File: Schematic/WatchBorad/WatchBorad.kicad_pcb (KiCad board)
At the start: 4 copper layers, 35 x 35 mm, 118 parts, among them J1 Conn_01x07_Female, J3 TYPE-C-31-M-17, M1 Motor_DC, SW1 SW_Push, SW2 SW_Push, SW3 SW_Push, SW4 SW_Push, SW5 SW_Push, U1 LSM6DSLTR, U10 TPS62740DSST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

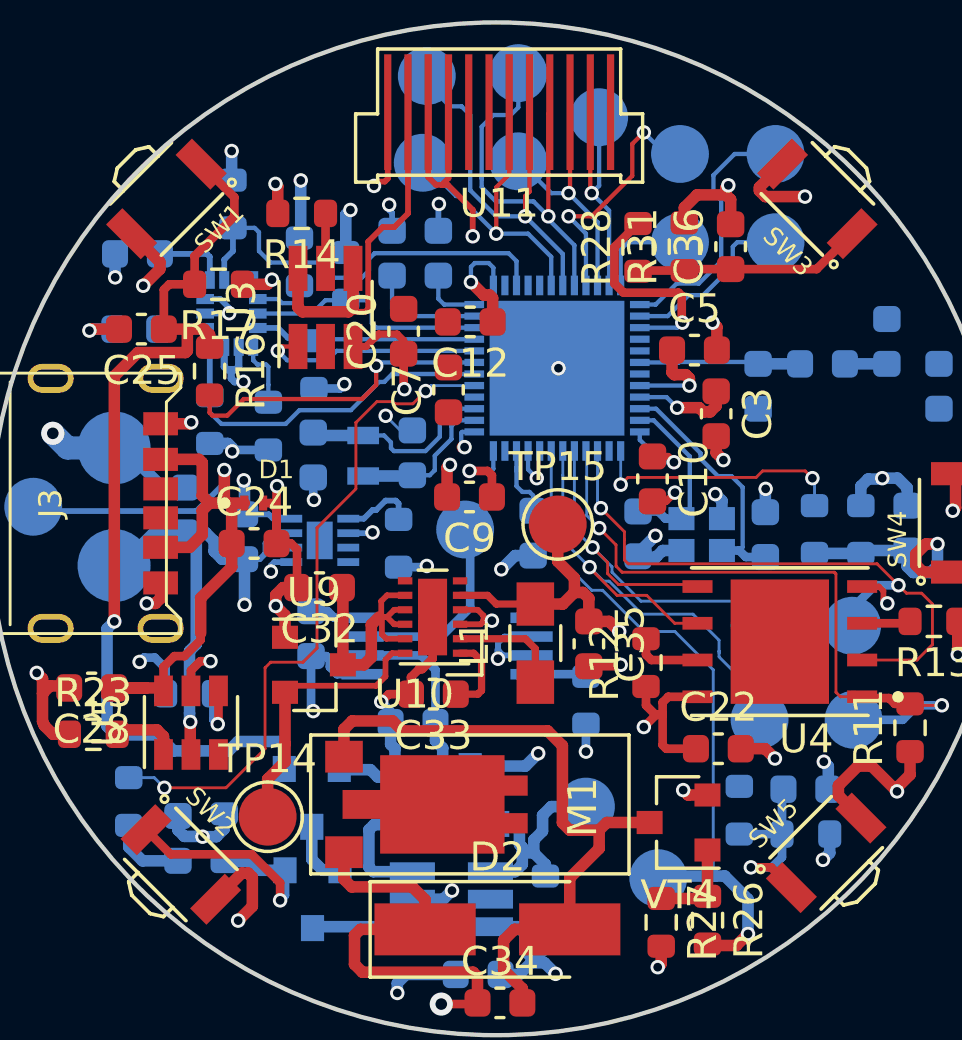
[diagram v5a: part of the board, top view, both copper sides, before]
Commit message: Fixed DRC warnings
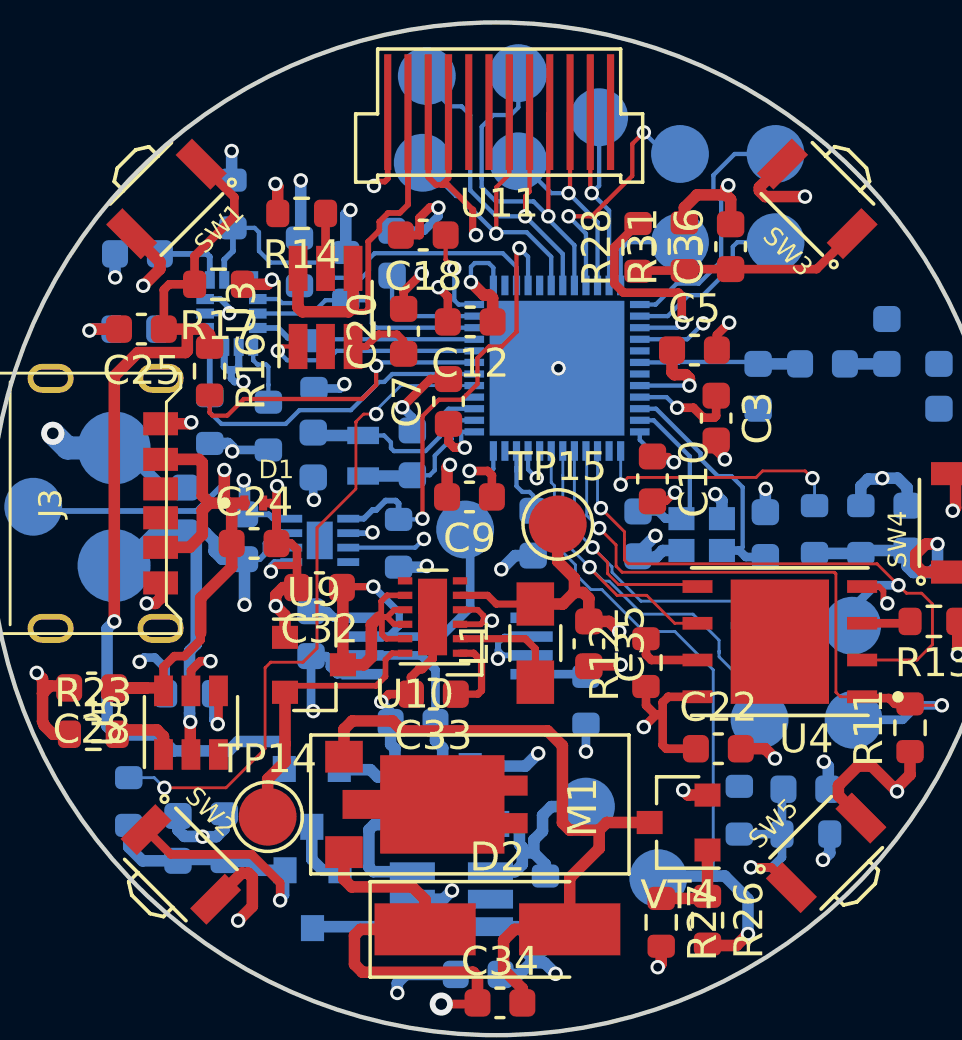
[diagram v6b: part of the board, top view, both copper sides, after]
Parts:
- C18: moved to F.Cu
- moved C18 0.82 mm to (86.4, 78.8), turned to 180 degrees
- moved C7 0.40 mm to (87.2, 84.5)
- moved C3 0.15 mm to (96.5, 85.1)
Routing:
- net /MCU/FG_OD_ALRT_N: track 2.59 -> 16.3 mm, vias 0 -> 2
- net GND: track 92.6 -> 100.4 mm, vias 48 -> 49
- net /DCDC&PB/DCDC_VIN: track 19.9 -> 24.2 mm, vias 0 -> 1
- net /MCU/SCL_FG: track 0.00 -> 2.74 mm, vias 0 -> 1
- net /MCU/SDA_FG: track 0.00 -> 2.42 mm, vias 0 -> 1
- net Net-(C26-Pad1): track 12.0 -> 13.6 mm
- net +3V3: track 180.8 -> 182.4 mm, vias 19 -> 18
- net /MCU/DEC1: track 1.20 -> 2.48 mm
- net /MCU/NFC2: track 2.12 -> 3.13 mm, vias 0 -> 1
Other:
- rule via_min_size: 0.4 -> 0.5

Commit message: Added RTC to the schematic and PCB lists [PCB]
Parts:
- added U12: M41T62Q6F, M41T62Q6F:QFN50P300X300X100-17N, F.Cu at (75.6, 68.2)
- added Y1: Crystal_Small, Crystal:Crystal_SMD_3215-2Pin_3.2x1.5mm, F.Cu at (70.7, 67.5)
- X2: footprint Crystals:Crystal_SMD_2012-2pin_2.0x1.2mm -> Crystal:Crystal_SMD_3215-2Pin_3.2x1.5mm
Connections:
- net /MCU/MPU_SCL renamed /MCU/I2C_SCL
- net /MCU/MPU_SDA renamed /MCU/I2C_SDA
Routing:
- net /MCU/PB_1_MCU: track 23.5 -> 25.1 mm

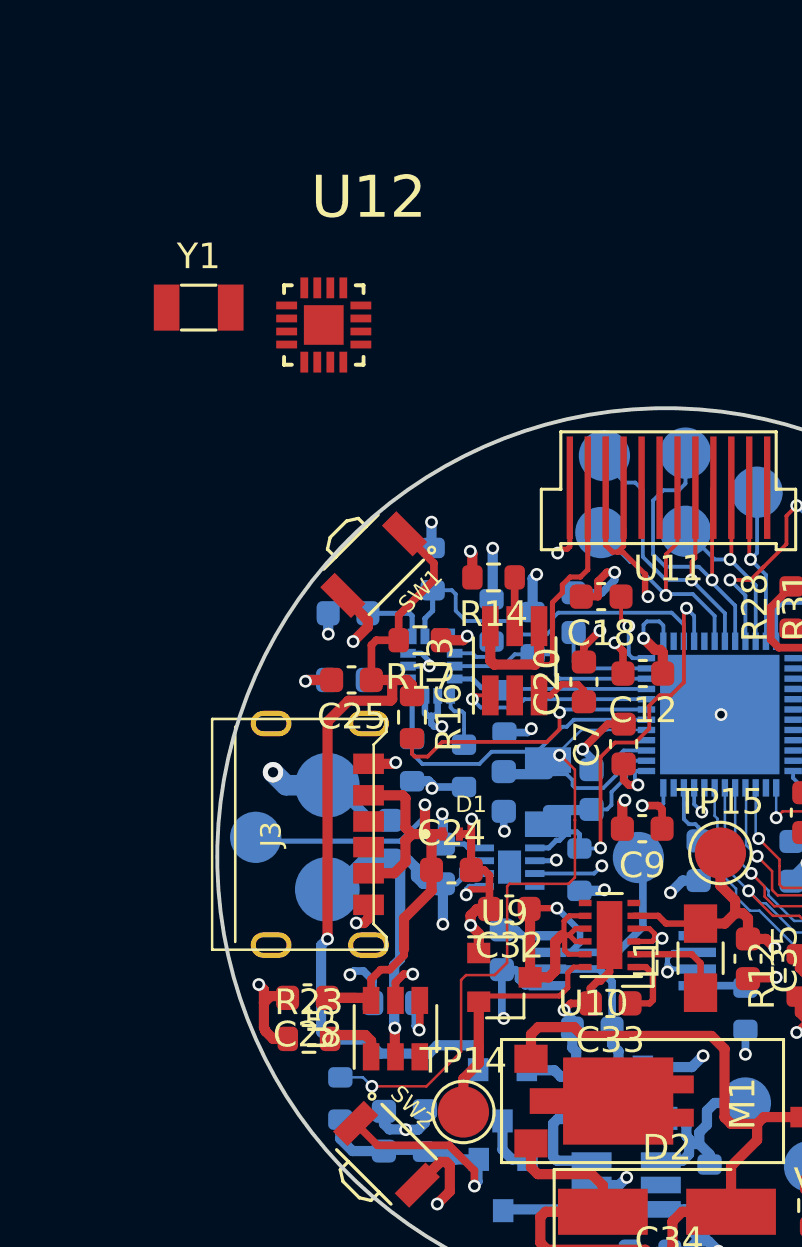
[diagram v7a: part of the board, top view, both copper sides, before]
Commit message: Added pull-up resistors for I2C bus. Refactored PCB for the Front layer
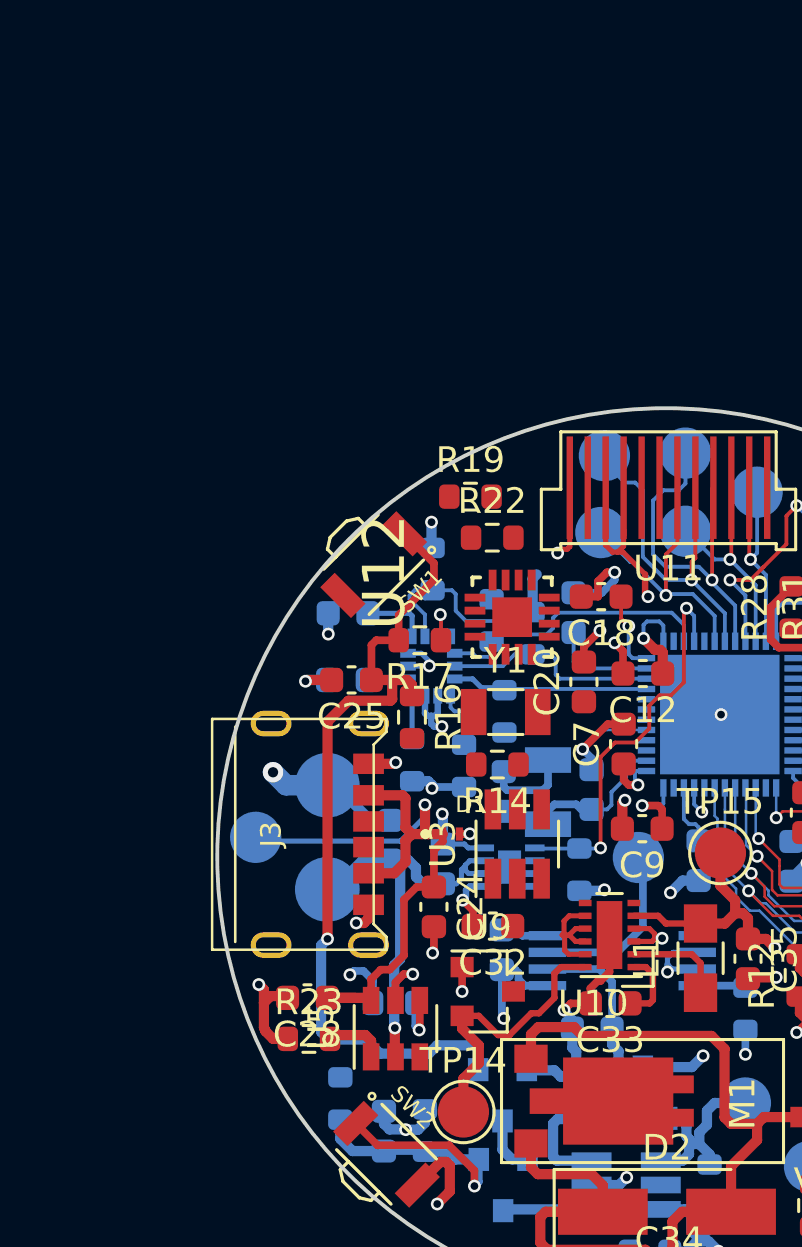
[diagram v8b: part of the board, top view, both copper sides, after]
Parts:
- added R19: 10k, Resistor_SMD:R_0603_1608Metric, F.Cu at (81.3, 74.8)
- added R22: 10k, Resistor_SMD:R_0603_1608Metric, F.Cu at (82.1, 76.5)
- moved Y1 19.8 mm to (82.7, 83.2)
- moved U12 13.6 mm to (82.9, 79.5), turned to 90 degrees
- moved R14 7.30 mm to (82.3, 85.3)
- moved U3 7.15 mm to (83.1, 88.4)
- moved C24 1.59 mm to (79.8, 90.8), turned to 270 degrees
- moved C32 0.93 mm to (82.2, 91.6)
- moved U9 0.85 mm to (82.0, 94.2)
- turned X2 to 270 degrees
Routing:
- net /MCU/PB_1_MCU: track 25.1 -> 1.65 mm, vias 2 -> 0
- net +3V3: track 182.4 -> 164.4 mm, vias 18 -> 15
- net +BATT: track 73.4 -> 55.4 mm, vias 6 -> 4
- net /MCU/LEDK: track 13.3 -> 0.00 mm
- net /MCU/PB_2_MCU: track 10.9 -> 0.00 mm, vias 1 -> 0
- net /MCU/MPU_INT_1: track 12.3 -> 1.68 mm
- net /DCDC&PB/DCDC_VIN: track 24.2 -> 14.7 mm, vias 1 -> 0
- net GND: track 100.4 -> 92.1 mm, vias 49 -> 47
- net /MCU/Backlight_EN_DIM: track 7.82 -> 0.00 mm, vias 1 -> 0
- net /MCU/XL2: track 7.30 -> 3.58 mm
- net /MCU/SCL_FG: track 2.74 -> 0.00 mm, vias 1 -> 0
- net Net-(R14-Pad1): track 1.90 -> 0.00 mm
- net /DCDC&PB/DCDC_ENABLE: track 9.60 -> 11.0 mm
- net /MCU/MPU_INT_2: track 14.6 -> 15.9 mm
- net /MCU/FG_OD_ALRT_N: track 16.3 -> 15.5 mm
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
